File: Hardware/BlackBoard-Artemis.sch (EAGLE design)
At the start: 76 parts, among them IC3 LM1117, J2 CORTEX_DEBUG, J3 POWER_JACKSUPER_BOMB_DIGITY, J5 USB C, Q1 1.1A/60V/600mΩ, U1 ARTEMIS_FULL, U2 SPH0641LM4H-1, U3 AP2112-3.3V, U4 SPH0641LM4H-1, U5 CH340C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

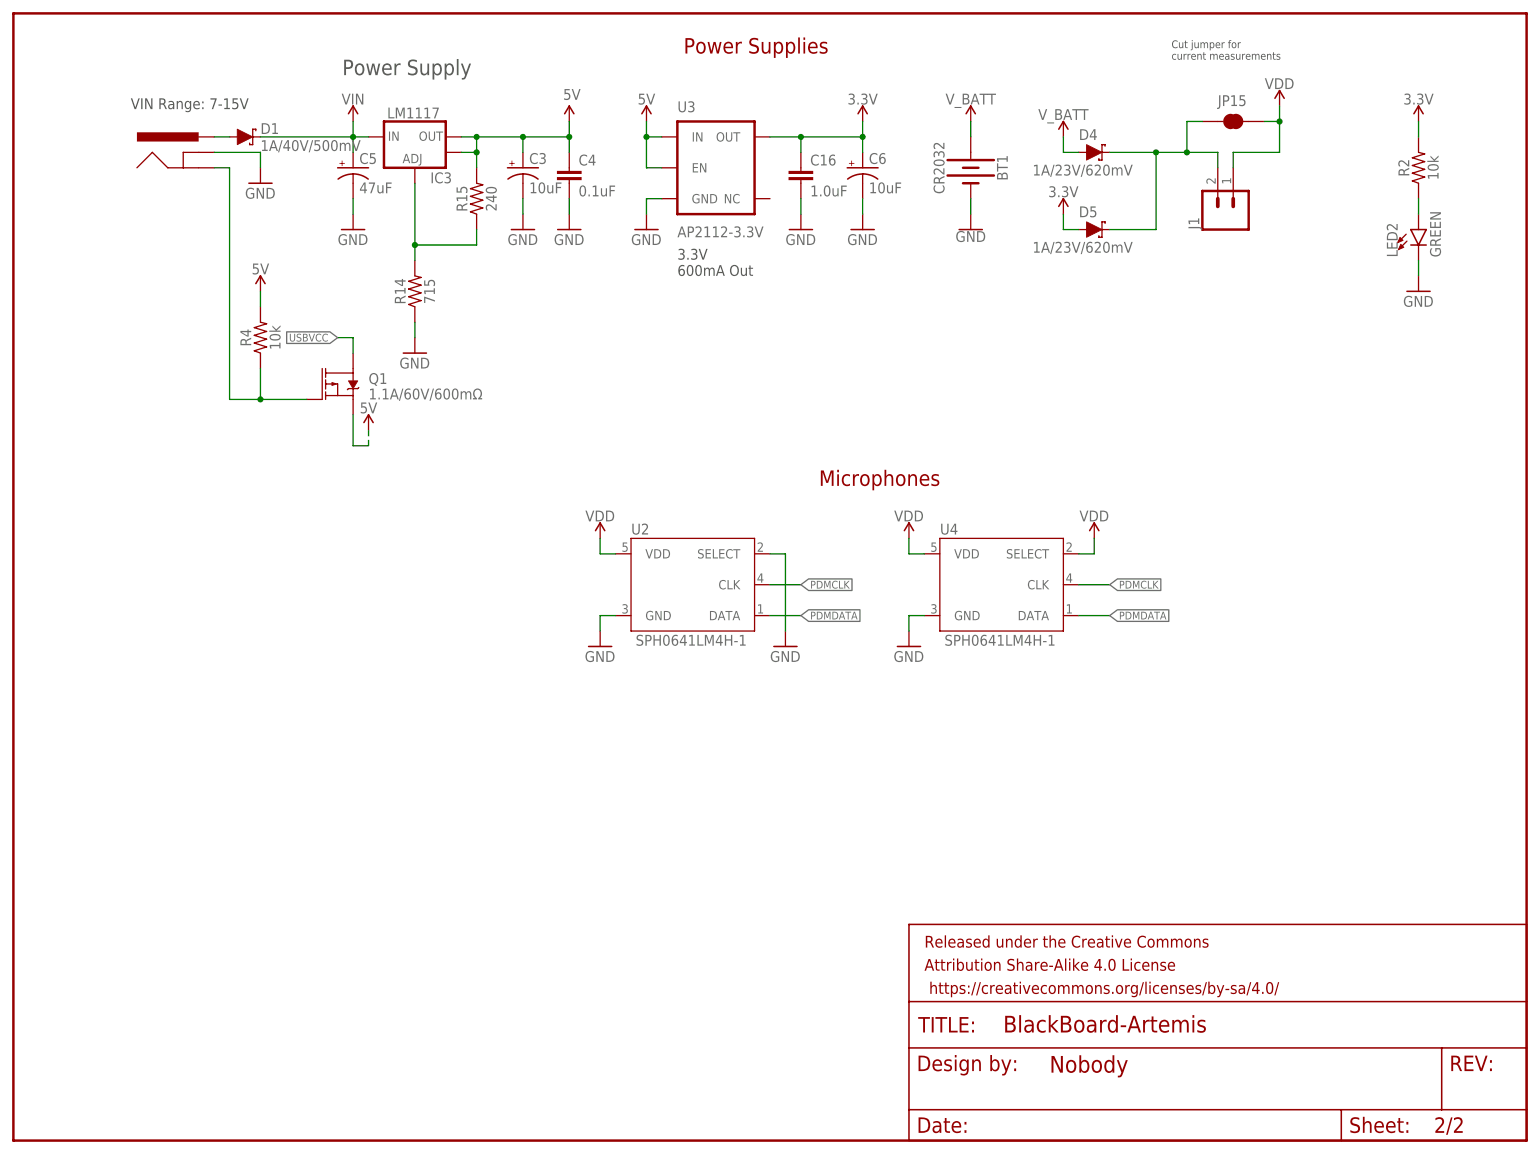
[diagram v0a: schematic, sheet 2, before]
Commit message: Fix I2C silk. Breakout UART0.
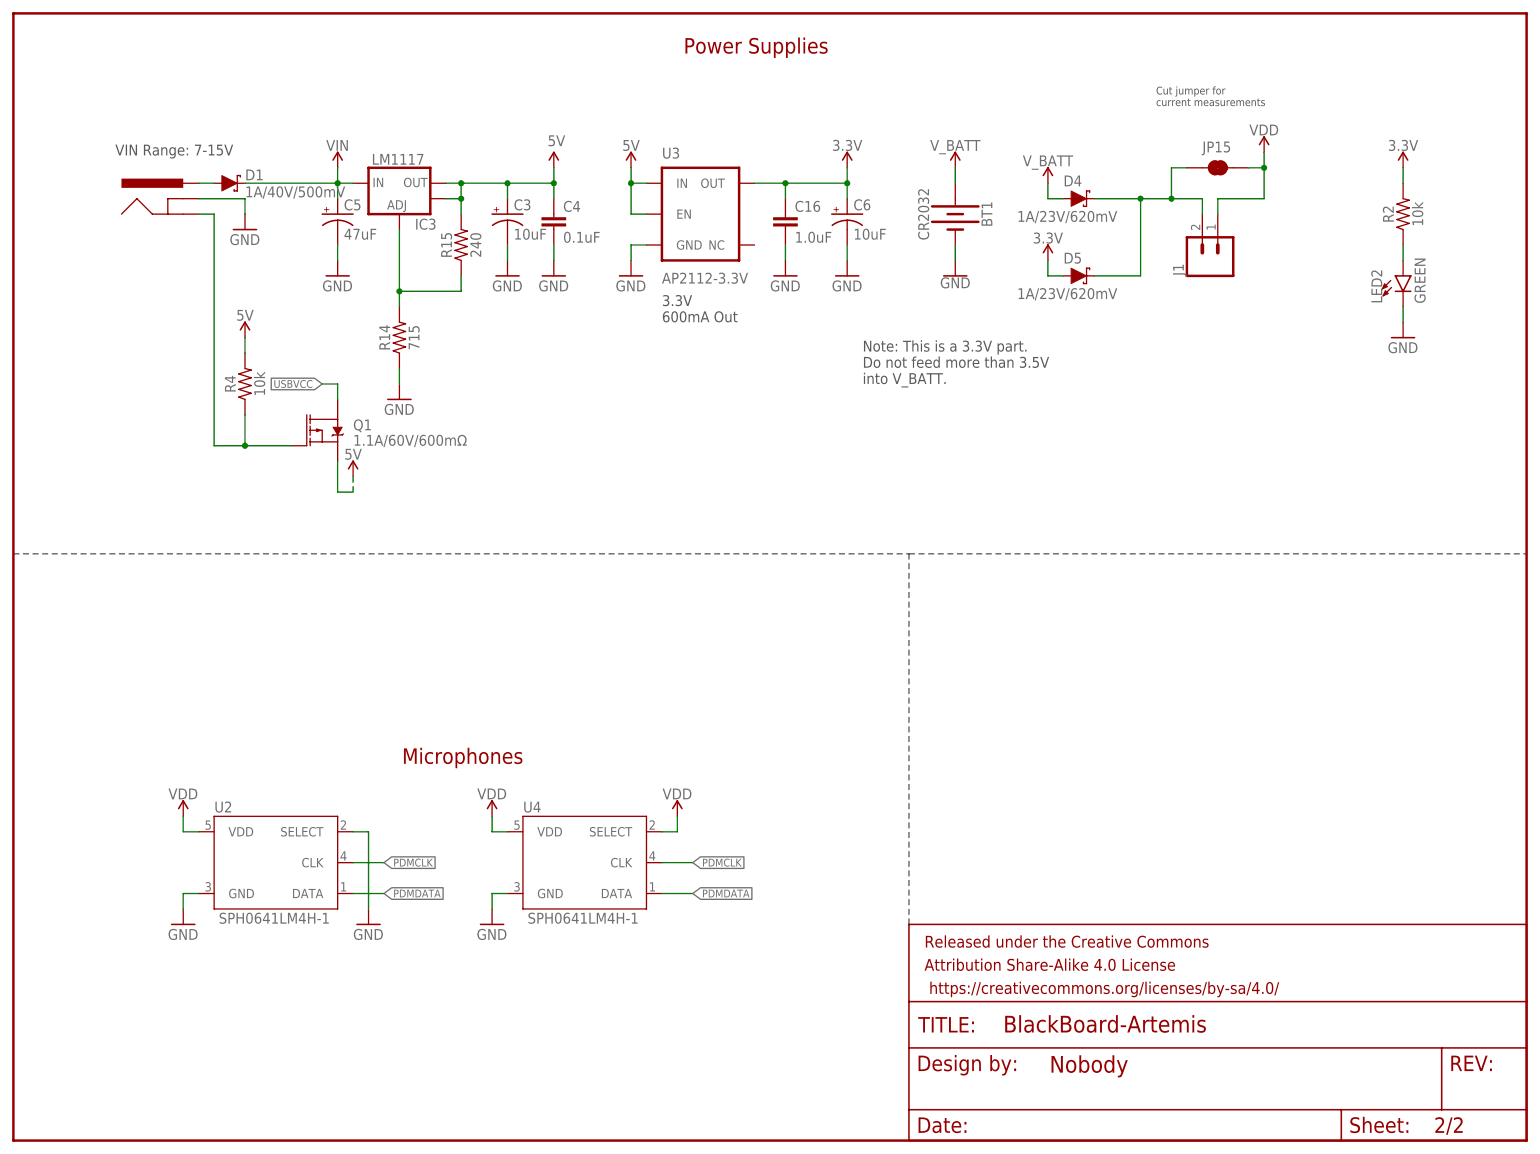
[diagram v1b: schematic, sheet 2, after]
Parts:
- added J7: (no value), SparkFun-Connectors:CONN_021X02_NO_SILK
- U1: value ARTEMIS_FULL -> ARTEMIS
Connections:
- net RXI-0: now also J7.1
- net TXO-0: now also J7.2
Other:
- note added: "Note: This is a 3.3V part. Do not feed more than 3.5V into V_BATT."
- note removed: "Power Supply"
- moved on the sheet: BT1, C16, C3, C4, C5, C6, D1, D4, D5, IC3, J1, JP15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

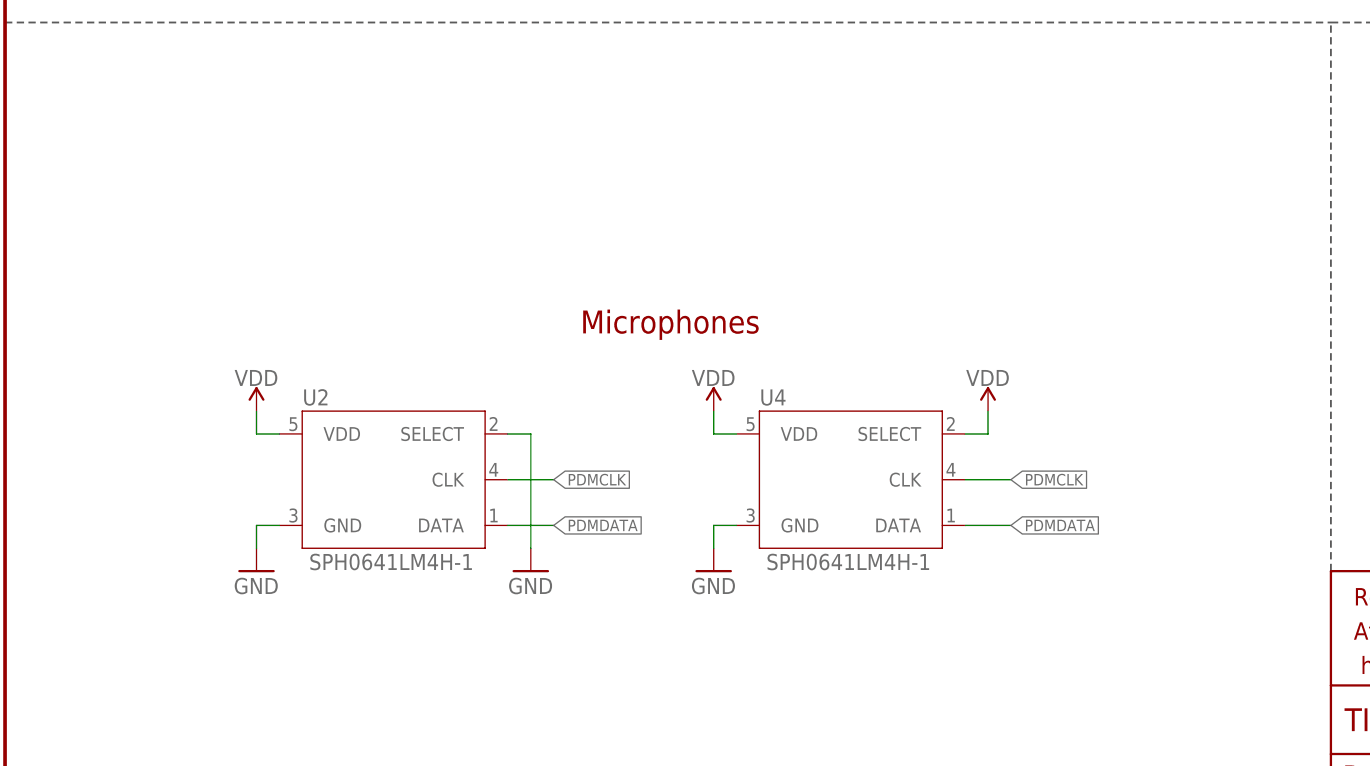
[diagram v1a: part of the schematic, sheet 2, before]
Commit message: Rev FP for mics. Add decoupling to mics.
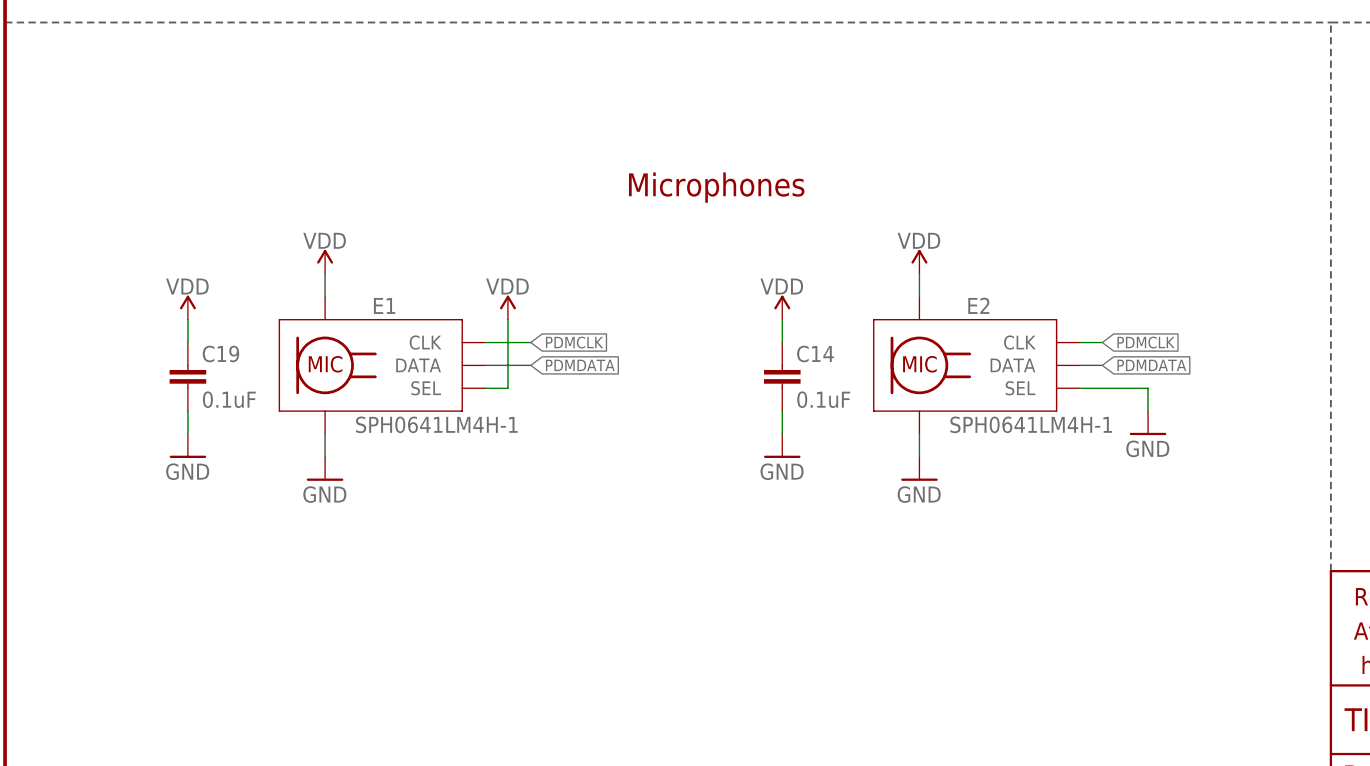
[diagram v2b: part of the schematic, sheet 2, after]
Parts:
- removed U1: ARTEMIS, Module-Pads:ARTEMIS_FULL
- removed U4: SPH0641LM4H-1, SparkFun-Sensors:SPH0641LM4H-1_MICROPHONE
- added C14, C19: 0.1uF, SparkFun-Capacitors:0.1UF-0603-25V-(+80/-20%)
- added C28: 1nF, SparkFun-Capacitors:1.0NF/1000PF-0603-50V-10%
- added E1, E2: SPH0641LM4H-1, SparkFun-Sensors:SPH0641LM4H-1_MICROPHONE
- J5: value USB C -> USB Female Type C Connector; device SparkFun-Connectors:USB_C16PIN -> SparkFun-Connectors:USB_C
- U2: value SPH0641LM4H-1 -> ARTEMIS_FULL; device SparkFun-Sensors:SPH0641LM4H-1_MICROPHONE -> Module-Pads:ARTEMIS_FULL
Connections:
- net !RESET: now also C28.1, U2.!RST; no longer U1.!RST
- net BOOT: now also U2.BOOT; no longer U1.BOOT
- net D11/MOSI: now also U2.MOSI; no longer U1.MOSI
- net D4: now also U2.D38; no longer U1.D38
- net GND: now also C14.2, C19.2, C28.2, E1.GND, E2.GND, E2.SEL; no longer U1.GND, U2.SELECT, U4.GND
- net N$7: now also U2.XI; no longer U1.XI
- net N$8: now also U2.XO; no longer U1.XO
- net PDMCLK: now also E1.CLK, E2.CLK, U2.D10; no longer U1.D10, U2.CLK, U4.CLK
- net PDMDATA: now also E1.DATA, E2.DATA, U2.D36; no longer U1.D36, U2.DATA, U4.DATA
- net RXI-0: now also U2.RXI-0; no longer U1.RXI-0
- net SDA: now also U2.SDA; no longer U1.SDA
- net SWDCK: now also U2.SWDCK; no longer U1.SWDCK
- net SWDIO: now also U2.SWDIO; no longer U1.SWDIO
- net TXO-0: now also U2.TXO-0; no longer U1.TXO-0
- net VDD: now also C14.1, C19.1, E1.SEL, E1.VDD, E2.VDD; no longer U1.VDD, U4.SELECT, U4.VDD
- net ~AD0: now also U2.~AD12; no longer U1.~AD12
- net ~AD1: now also U2.~AD13; no longer U1.~AD13
- net ~AD2: now also U2.~AD31; no longer U1.~AD31
- net ~AD3/SWO: now also U2.~AD33/SWO; no longer U1.~AD33/SWO
- net ~AD4: now also U2.~AD11; no longer U1.~AD11
- net ~AD5: now also U2.~AD29; no longer U1.~AD29
- net ~D10: now also U2.~D26; no longer U1.~D26
- net ~D12/MISO: now also U2.MISO; no longer U1.MISO
- net ~D13/SCK: now also U2.SCK; no longer U1.SCK
- net ~D14: now also U2.~D43; no longer U1.~D43
- net ~D15: now also U2.~D42; no longer U1.~D42
- net ~D16: now also U2.~D37; no longer U1.~D37
- net ~D2: now also U2.~D44; no longer U1.~D44
- net ~D3: now also U2.~D4; no longer U1.~D4
- net ~D5: now also U2.~D27; no longer U1.~D27
- net ~D6: now also U2.~D22; no longer U1.~D22
- net ~D7: now also U2.~AD35; no longer U1.~AD35
- net ~D8: now also U2.~AD32; no longer U1.~AD32
- net ~D9: now also U2.~D28; no longer U1.~D28
- net ~RXI-1: now also U2.TX1; no longer U1.TX1
- net ~SCL: now also U2.SCL; no longer U1.SCL
- net ~TXO-1: now also U2.RX1; no longer U1.RX1

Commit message: Update power jack. Change to PDM mics.
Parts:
- J3: value POWER_JACKSUPER_BOMB_DIGITY -> POWER_JACKTOE; device Testing:POWER_JACKSUPER_BOMB_DIGITY -> SparkFun-Connectors:POWER_JACKTOE
- J5: value USB Female Type C Connector -> USB-C
- LED1: value Blue -> BLUE; device SparkFun-LED:LED-BLUE_HIDDENSILK -> SparkFun-LED:LED-BLUE1206
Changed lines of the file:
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@@
 <part name="SUPPLY5" library="SparkFun-PowerSymbols" deviceset="VIN" device=""/>
 <part name="GND26" library="SparkFun-PowerSymbols" deviceset="GND" device=""/>
-<part name="LED1" library="SparkFun-LED" deviceset="LED-BLUE" device="_HIDDENSILK" value="Blue">
+<part name="LED1" library="SparkFun-LED" deviceset="LED-BLUE" device="1206" value="BLUE">
 <attribute name="PROD_ID" value="DIO-09911"/>
 </part>
@@
 <part name="J4" library="SparkFun-Connectors" deviceset="QWIIC_CONNECTOR" device="JS-1MM"/>
 <part name="GND2" library="SparkFun-PowerSymbols" deviceset="GND" device=""/>
-<part name="J5" library="SparkFun-Connectors" deviceset="USB_C" device="" value="USB Female Type C Connector"/>
+<part name="J5" library="SparkFun-Connectors" deviceset="USB_C" device="" value="USB-C"/>
 <part name="GND38" library="SparkFun-PowerSymbols" deviceset="GND" device=""/>
 <part name="U5" library="SparkFun-IC-Comms" deviceset="CH340C" device=""/>
@@
 <part name="SUPPLY7" library="SparkFun-PowerSymbols" deviceset="VIN" device=""/>
 <part name="D1" library="SparkFun-DiscreteSemi" deviceset="DIODE-SCHOTTKY" device="-SS14" value="1A/40V/500mV"/>
-<part name="J3" library="Testing" deviceset="POWER_JACK" device="SUPER_BOMB_DIGITY">
+<part name="J3" library="SparkFun-Connectors" deviceset="POWER_JACK" device="TOE">
 <attribute name="PROD_ID" value="CONN-08106"/>
 </part>

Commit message: Change 10nF to 0.1uF on auto reset circuit
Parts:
- C8: value 10nF -> 0.1uF; device SparkFun-Capacitors:10NF-0603-50V-10% -> SparkFun-Capacitors:0.1UF-0603-25V-(+80/-20%)
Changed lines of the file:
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@@
 <part name="C2" library="SparkFun-Capacitors" deviceset="0.1UF" device="-0603-25V-(+80/-20%)" value="0.1uF"/>
 <part name="GND7" library="SparkFun-PowerSymbols" deviceset="GND" device=""/>
-<part name="C8" library="SparkFun-Capacitors" deviceset="10NF" device="-0603-50V-10%" value="10nF"/>
+<part name="C8" library="SparkFun-Capacitors" deviceset="0.1UF" device="-0603-25V-(+80/-20%)" value="0.1uF"/>
 <part name="C10" library="SparkFun-Capacitors" deviceset="0.1UF" device="-0603-25V-(+80/-20%)" value="0.1uF"/>
 <part name="GND24" library="SparkFun-PowerSymbols" deviceset="GND" device=""/>

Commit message: Change 10nF to 0.1uF on auto-reset circuit
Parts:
- C8: device SparkFun-Capacitors:0.1UF-0603-25V-(+80/-20%) -> SparkFun-Capacitors:0.1UF-0603-25V-5%
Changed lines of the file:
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@@
 <part name="C2" library="SparkFun-Capacitors" deviceset="0.1UF" device="-0603-25V-(+80/-20%)" value="0.1uF"/>
 <part name="GND7" library="SparkFun-PowerSymbols" deviceset="GND" device=""/>
-<part name="C8" library="SparkFun-Capacitors" deviceset="0.1UF" device="-0603-25V-(+80/-20%)" value="0.1uF"/>
+<part name="C8" library="SparkFun-Capacitors" deviceset="0.1UF" device="-0603-25V-5%" value="0.1uF"/>
 <part name="C10" library="SparkFun-Capacitors" deviceset="0.1UF" device="-0603-25V-(+80/-20%)" value="0.1uF"/>
 <part name="GND24" library="SparkFun-PowerSymbols" deviceset="GND" device=""/>

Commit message: Version x02 - now uses Artemis v10. One mic, more GPIO, better silk,
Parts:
- removed C14: 0.1uF, SparkFun-Capacitors:0.1UF-0603-25V-(+80/-20%)
- removed E2: SPH0641LM4H-1, SparkFun-Sensors:SPH0641LM4H-1_MICROPHONE
- removed J6: (no value), SparkFun-Connectors:CONN_031X03_NO_SILK
- removed U2: ARTEMIS_FULL, Module-Pads:ARTEMIS_FULL
- added JP16: JUMPER-SMT_2_NC_TRACE_SILK, SparkFun-Jumpers:JUMPER-SMT_2_NC_TRACE_SILK
- added TP11, TP12, TP13, TP14, TP8, TP9: TEST-POINT3X5, SparkFun-Connectors:TEST-POINT3X5
- added U4: ARTEMIS_MODULESMD, Testing:ARTEMIS_MODULESMD
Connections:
- removed net D11/MOSI: JP2.7, U2.MOSI
- removed net D4: JP11.5, U2.D38
- removed net SDA: J4.3, JP2.2, U2.SDA
- removed net ~AD0: JP13.1, U2.~AD12
- removed net ~AD1: JP13.2, U2.~AD13
- removed net ~AD2: JP13.3, U2.~AD31
- removed net ~AD4: JP13.5, U2.~AD11
- removed net ~AD5: JP13.6, U2.~AD29
- removed net ~D10: JP2.8, U2.~D26
- removed net ~D12/MISO: JP2.6, U2.MISO
- removed net ~D13/SCK: JP2.5, R1.1, U2.SCK
- removed net ~D14: J6.1, U2.~D43
- removed net ~D15: J6.2, U2.~D42
- removed net ~D16: J6.3, U2.~D37
- removed net ~D2: JP11.3, U2.~D44
- removed net ~D3: JP11.4, U2.~D4
- removed net ~D5: JP11.6, U2.~D27
- removed net ~D6: JP11.7, U2.~D22
- removed net ~D7: JP11.8, U2.~AD35
- removed net ~D8: JP2.10, U2.~AD32
- removed net ~D9: JP2.9, U2.~D28
- removed net ~RXI-1: JP11.1, U2.TX1
- removed net ~SCL: J4.4, JP2.1, U2.SCL
- removed net ~TXO-1: JP11.2, U2.RX1
- new net AD16: JP13.5, U4.AD16(CMPIN0)
- new net AD34: JP13.3, U4.AD34(CMPRF2)
- new net D10: TP14.1, U4.(MOSI1/TX1/PDMCLK)D10
- new net D38: TP11.1, U4.(MOSI3/RX1)D38
- new net D40/SDA: J4.3, JP2.2, U4.(SDA4/MISO4/RX1)D40
- new net D7/MOSI: JP2.7, U4.(MOSI0/CLKOUT)D7
- new net D8: TP12.1, U4.(SCL1/SCK1/TX1/SCCLK)D8
- new net D9: TP13.1, U4.(SDA1/MISO1/RX1/SCCIO)D9
- new net N$10: JP16.2, JP2.3
- new net ~AD11: JP13.2, U4.~AD11
- new net ~AD12: JP2.9, U4.~AD12
- new net ~AD13: JP2.8, U4.~AD13(I2S)
- new net ~AD29: JP13.1, U4.~AD29(PDMDATA)
- new net ~AD31: JP13.6, U4.~AD31(RTS1/SCCLK)
- new net ~AD32: JP2.10, U4.~AD32(SCIO)
- new net ~AD35: JP11.3, U4.~AD35(I2SDAT)
- new net ~D22: JP11.5, U4.(PDMCLK)~D22
- new net ~D23: JP11.6, U4.(CMPOUT)~D23
- new net ~D24/TXO-1: JP11.2, U4.(TX1/32KHZ)~D24
- new net ~D25/RXI-1: JP11.1, U4.(SDA2/MISO2/RX1)~D25
- new net ~D27: JP11.7, U4.(SCL2/SCK2)~D27
- new net ~D28: JP11.8, U4.(MOSI2/I2SWCLK)~D28
- new net ~D39/SCL: J4.4, JP2.1, U4.(SCL4/SCK4/TX1)~D39
- new net ~D4: JP11.4, U4.(RX1)~D4
- new net ~D42: TP9.1, U4.(SCL3/SCK3/TX1)~D42
- new net ~D43: TP8.1, U4.(SDA3/MISO3/RX1)~D43
- new net ~D5/SCK: JP2.5, R1.1, U4.(SCL0/SCK0)~D5
- new net ~D6/MISO: JP2.6, U4.(SDA0/MISO0/I2SDAT)~D6
- net !RESET: now also U4.!RST; no longer U2.!RST
- net BOOT: now also U4.BOOT(P/MOSI5/RX1/32KHZ); no longer U2.BOOT
- net GND: now also JP16.1, U4.GND*6; no longer C14.2, E2.GND, E2.SEL, U2.GND
- net N$7: now also U4.XO; no longer U2.XI
- net N$8: now also U4.XI; no longer U2.XO
- net PDMCLK: now also U4.(PDMCLK/SCCIO)~D37; no longer E2.CLK, U2.D10
- net PDMDATA: now also U4.(RX1/PDMDATA)D36; no longer E2.DATA, U2.D36
- net RXI-0: now also U4.RX0(P/SDA5/MISO5); no longer U2.RXI-0
- net SWDCK: now also U4.SWDCK; no longer U2.SWDCK
- net SWDIO: now also U4.SWDIO; no longer U2.SWDIO
- net TXO-0: now also U4.TX0(P/SCL5/SCK5); no longer U2.TXO-0
- net VDD: now also U4.VDD*2; no longer C14.1, E2.VDD, U2.VDD
- net ~AD3/SWO: now also U4.~AD33(SWO); no longer U2.~AD33/SWO
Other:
- moved on the sheet: C11, C13, J2, LED1, R1, TP1, TP2, TP3, Y1
